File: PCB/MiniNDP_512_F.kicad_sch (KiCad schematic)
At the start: 15 parts, among them J1 Conn_02x20_Odd_Even, U1 HC238, U2 HC4040, U3 FCT841, U4 AS6C4008, U5 HC00

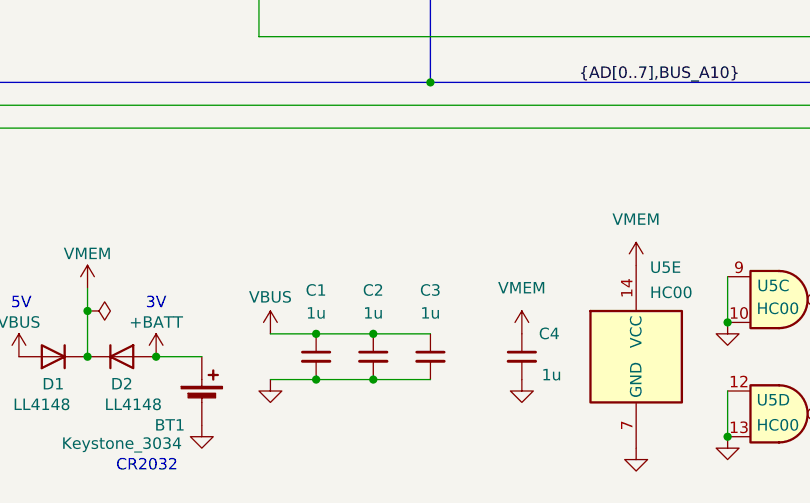
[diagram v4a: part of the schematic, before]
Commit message: easy boards add 47u cap, remove ramrst diode
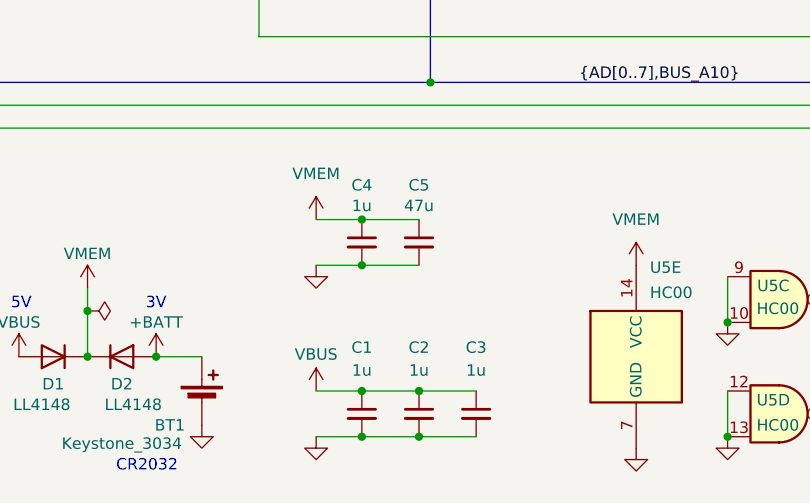
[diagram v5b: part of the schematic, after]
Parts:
- added C5: 47u, 000_LOCAL:C_1206, symbol 000_LOCAL:C
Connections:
- net GND: now also C5.2
- net VMEM: now also C5.1
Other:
- moved on the sheet: C1, C2, C3, C4
